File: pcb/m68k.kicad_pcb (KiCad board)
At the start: 2 copper layers, 89 parts, among them J1 USB_B_Micro, J4 DB15_Male_HighDensity, U1 93LC56, U10 25LCxxx, U11 TXB0108DQSR, U12 TXB0108DQSR, U13 iCE40-HX4K-TQ144, U14 ADV7125KSTZ50, U15 74LVC1G17, U16 LD1117S33TR_SOT223, U17 LD1117S12TR_SOT223, U2 68000D, U3 FT2232H, U4 TXB0108DQSR, U5 TXB0108DQSR, U6 TXB0108DQSR, U7 SN74LVC8T245PWR, U8 SN74LVC8T245PWR, U9 AS6C1616, X1 ASV-12.000MHz

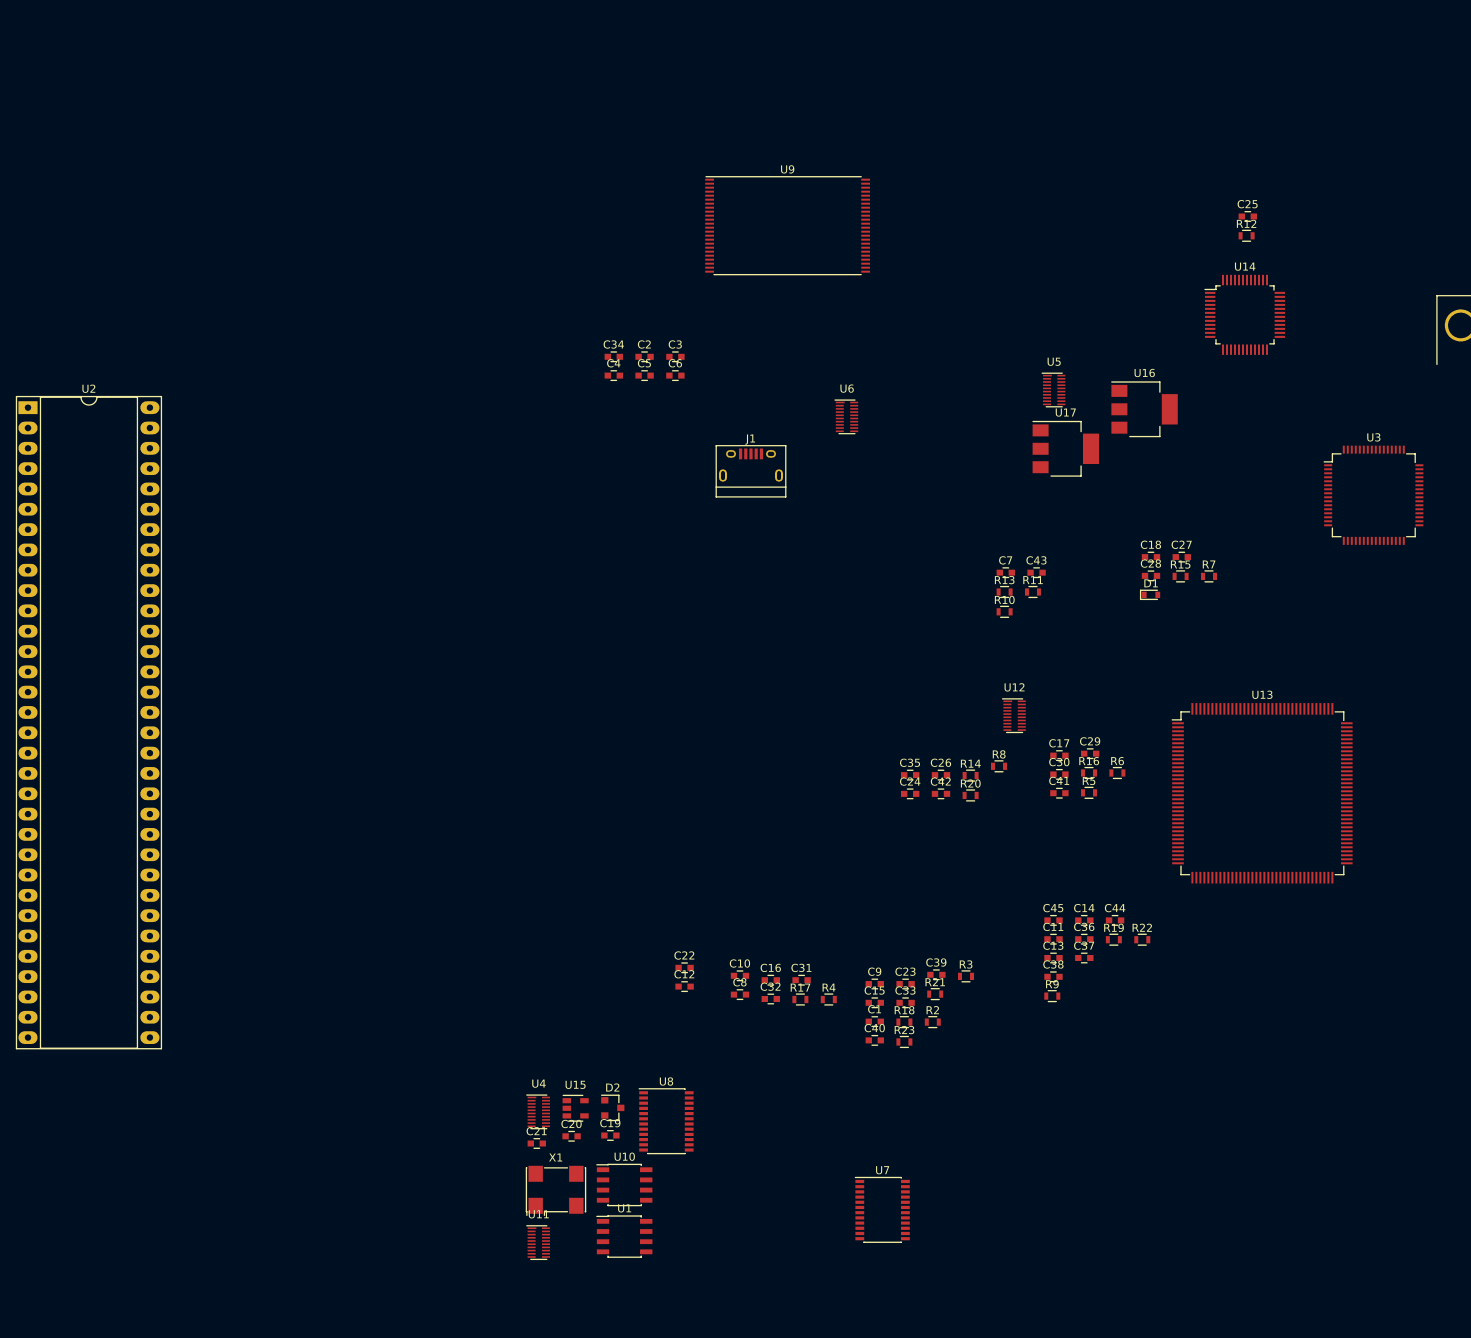
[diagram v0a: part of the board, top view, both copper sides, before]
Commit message: Reordered U8 Pins
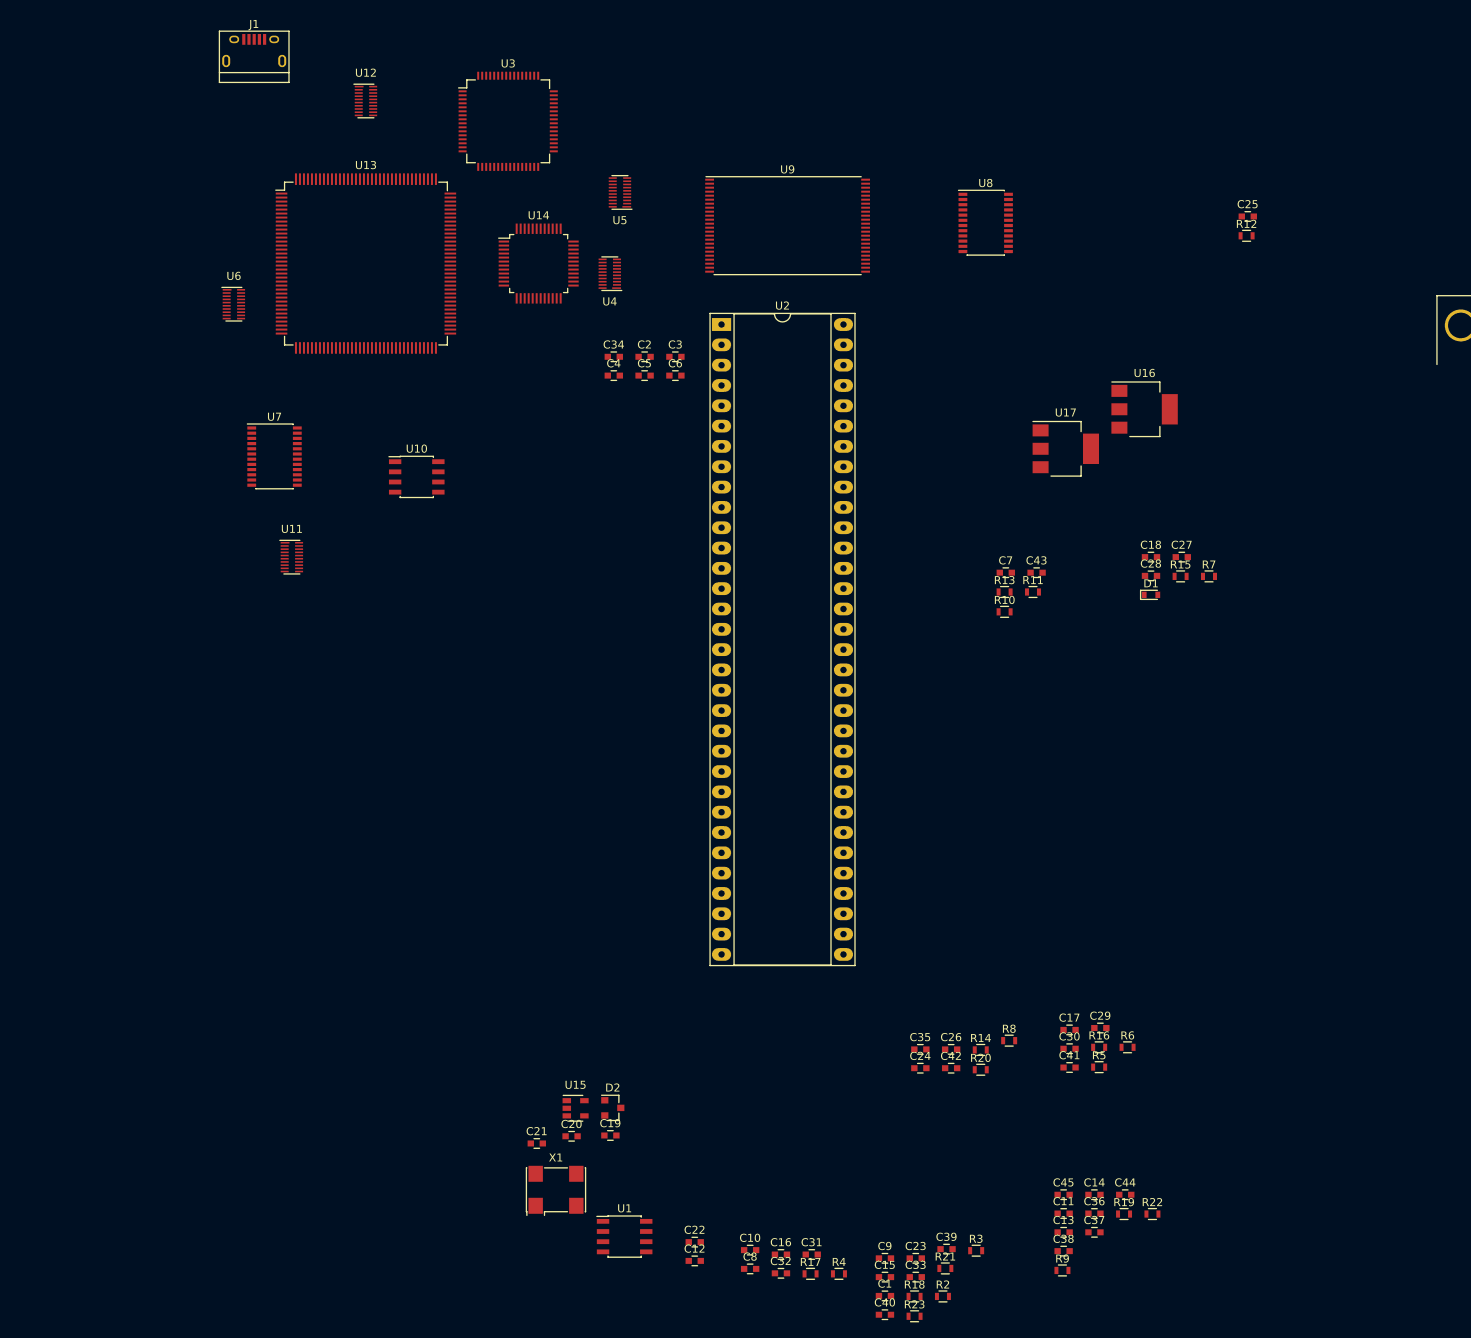
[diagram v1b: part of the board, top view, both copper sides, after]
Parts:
- moved U13 130.2 mm to (71.1, 61.0)
- moved U7 121.0 mm to (59.7, 85.1)
- moved U8 119.2 mm to (148.6, 55.9)
- moved U3 117.9 mm to (88.9, 43.2)
- moved U12 111.7 mm to (71.1, 40.6)
- moved U4 105.1 mm to (101.6, 62.2), turned to 180 degrees
- moved U10 92.2 mm to (77.5, 87.6)
- moved U11 91.1 mm to (61.9, 97.7)
- moved U14 88.5 mm to (92.7, 61.0)
- moved U2 87.3 mm to (115.6, 68.6)
- moved J1 80.9 mm to (57.1, 34.3)
- moved U6 77.9 mm to (54.6, 66.0)
- moved U5 59.6 mm to (102.9, 52.1), turned to 180 degrees
- moved C11 34.3 mm to (158.3, 179.7)
- moved C16 34.3 mm to (123.0, 184.8)
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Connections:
- U8 pad 10: /d15 -> /d8
- U8 pad 14: /D15 -> /D8
- U8 pad 15: /D14 -> /D9
- U8 pad 16: /D13 -> /D10
- U8 pad 17: /D12 -> /D11
- U8 pad 18: /D11 -> /D12
- U8 pad 19: /D10 -> /D13
- U8 pad 20: /D9 -> /D14
- U8 pad 21: /D8 -> /D15
- U8 pad 3: /d8 -> /d15
- U8 pad 4: /d9 -> /d14
- U8 pad 5: /d10 -> /d13
- U8 pad 6: /d11 -> /d12
- U8 pad 7: /d12 -> /d11
- U8 pad 8: /d13 -> /d10
- U8 pad 9: /d14 -> /d9
